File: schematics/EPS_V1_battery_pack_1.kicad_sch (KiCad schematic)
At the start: 31 parts, among them U1 MP2672AGD-0000-Z, U5 MAX17205G+

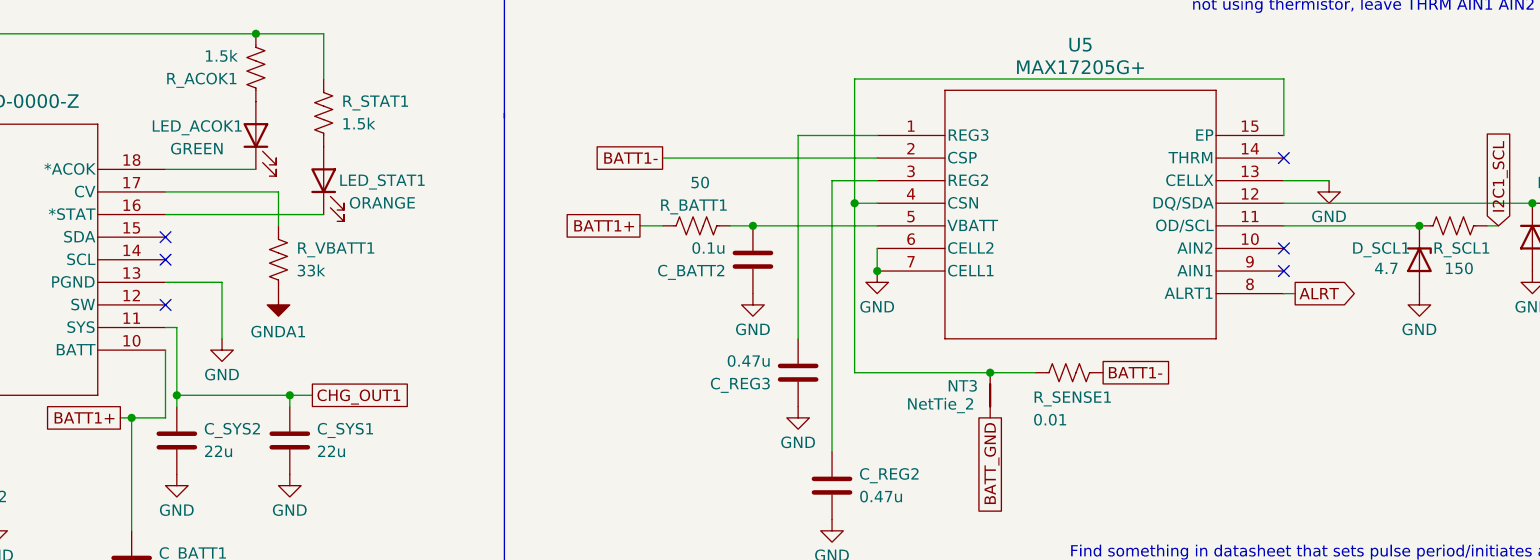
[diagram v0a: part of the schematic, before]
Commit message: Fix NC pins, add 2 test points & silkscreen labels
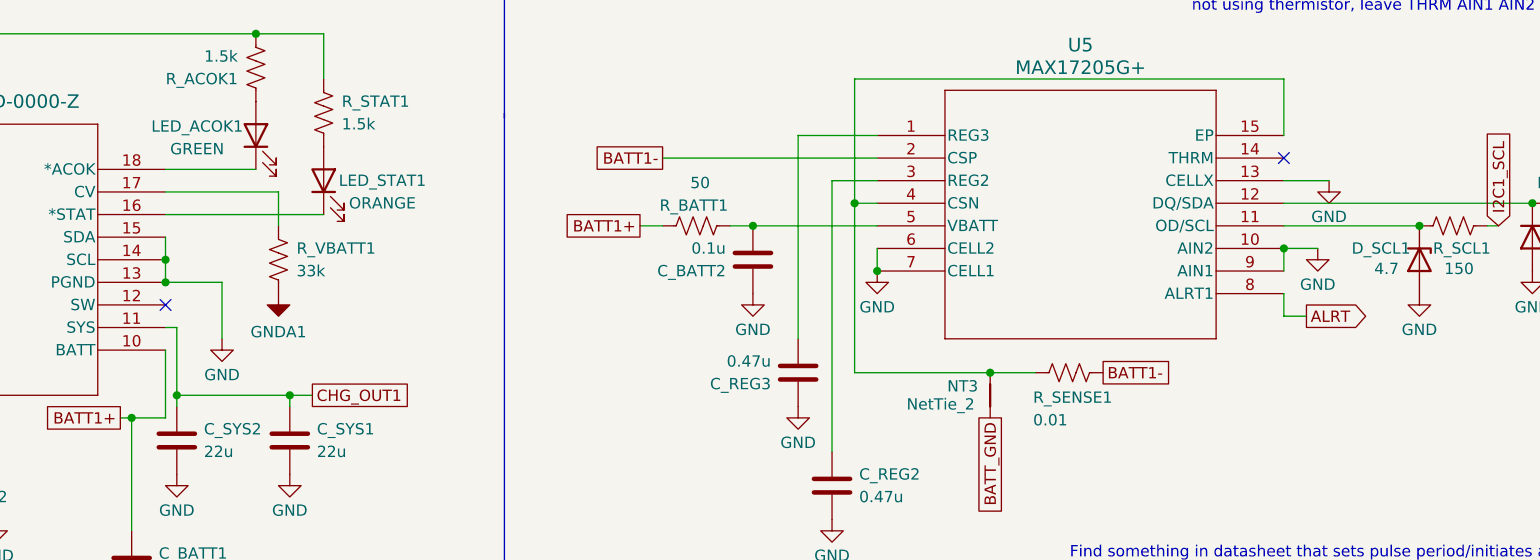
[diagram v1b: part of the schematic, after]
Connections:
- net GND: now also U1.14 (SCL), U1.15 (SDA), U5.10 (AIN2), U5.9 (AIN1)
- no-connect marks 6 -> 2
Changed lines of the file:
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@@
+	)
+	(junction
+		(at 104.14 91.44)
+		(diameter 0)
+		(color 0 0 0 0)
 	)
 	(junction
@@
 	)
 	(junction
+		(at 229.87 87.63)
+		(diameter 0)
+		(color 0 0 0 0)
+	)
+	(junction
 		(at 170.18 85.09)
 		(diameter 0)
@@
 	)
 	(junction
+		(at 104.14 88.9)
+		(diameter 0)
+		(color 0 0 0 0)
+	)
+	(junction
 		(at 50.8 96.52)
 		(diameter 0)
@@
 	)
 	(no_connect
-		(at 229.87 90.17)
-	)
-	(no_connect
 		(at 104.14 93.98)
-	)
-	(no_connect
-		(at 104.14 88.9)
-	)
-	(no_connect
-		(at 104.14 86.36)
 	)
 	(no_connect
 		(at 229.87 77.47)
 	)
-	(no_connect
-		(at 229.87 87.63)
-	)
 	(wire
 		(pts
@@
 	(wire
 		(pts
+			(xy 229.87 87.63) (xy 233.68 87.63)
+		)
+		(stroke
+			(width 0)
+			(type default)
+		)
+	)
+	(wire
+		(pts
 			(xy 50.8 86.36) (xy 63.5 86.36)
 		)
@@
 	(wire
 		(pts
+			(xy 104.14 86.36) (xy 104.14 88.9)
+		)
+		(stroke
+			(width 0)
+			(type default)
+		)
+	)
+	(wire
+		(pts
 			(xy 170.18 85.09) (xy 184.15 85.09)
 		)
@@
 		)
 	)
+	(wire
+		(pts
+			(xy 229.87 95.25) (xy 229.87 92.71)
+		)
+		(stroke
+			(width 0)
+			(type default)
+		)
+	)
 	(polyline
 		(pts
@@
 	(wire
 		(pts
+			(xy 229.87 87.63) (xy 229.87 90.17)
+		)
+		(stroke
+			(width 0)
+			(type default)
+		)
+	)
+	(wire
+		(pts
 			(xy 50.8 96.52) (xy 50.8 95.25)
 		)
@@
 	(wire
 		(pts
-			(xy 229.87 92.71) (xy 231.14 92.71)
-		)
-		(stroke
-			(width 0)
-			(type default)
-		)
-	)
-	(wire
-		(pts
 			(xy 104.14 83.82) (xy 121.92 83.82)
 		)
@@
 	(wire
 		(pts
+			(xy 229.87 95.25) (xy 232.41 95.25)
+		)
+		(stroke
+			(width 0)
+			(type default)
+		)
+	)
+	(wire
+		(pts
 			(xy 29.21 93.98) (xy 63.5 93.98)
 		)
@@
 		(pts
 			(xy 114.3 63.5) (xy 48.26 63.5)
+		)
+		(stroke
+			(width 0)
+			(type default)
+		)
+	)
+	(wire
+		(pts
+			(xy 104.14 88.9) (xy 104.14 91.44)
 		)
 		(stroke
@@
 	(global_label "ALRT"
 		(shape output)
-		(at 231.14 92.71 0)
+		(at 232.41 95.25 0)
 		(fields_autoplaced yes)
 		(effects
@@
 		)
 		(property "Intersheetrefs" "${INTERSHEET_REFS}"
-			(at 238.4795 92.71 0)
+			(at 239.7495 95.25 0)
 			(hide yes)
 			(show_name no)
@@
 					(unit 1)
 				)
+			)
+		)
+	)
+	(symbol
+		(lib_id "power:GND")
+		(at 233.68 87.63 0)
+		(unit 1)
+		(body_style 1)
+		(exclude_from_sim no)
+		(in_bom yes)
+		(on_board yes)
+		(in_pos_files yes)
+		(dnp no)
+		(property "Reference" "#PWR0130"
+			(at 233.68 93.98 0)
+			(hide yes)
+			(show_name no)
+			(do_not_autoplace no)
+			(effects
+				(font
+					(size 1.27 1.27)
+				)
+			)
+		)
+		(property "Value" "GND"
+			(at 233.68 91.694 0)
+			(show_name no)
+			(do_not_autoplace no)
+			(effects
+				(font
+					(size 1.27 1.27)
+				)
+			)
+		)
+		(property "Footprint" ""
+			(at 233.68 87.63 0)
+			(hide yes)
+			(show_name no)
+			(do_not_autoplace no)
+			(effects
+				(font
+					(size 1.27 1.27)
+				)
+			)
+		)
+		(property "Datasheet" ""
+			(at 233.68 87.63 0)
+			(hide yes)
+			(show_name no)
+			(do_not_autoplace no)
+			(effects
+				(font
+					(size 1.27 1.27)
+				)
+			)
+		)
+		(property "Description" "Power symbol creates a global label with name \"GND\" , ground"
+			(at 233.68 87.63 0)
+			(hide yes)
+			(show_name no)
+			(do_not_autoplace no)
+			(effects
+				(font
+					(size 1.27 1.27)
+				)
+			)
+		)
+		(pin "1"
+		)
+		(instances
+			(project "EPS_V1"
+				(path "/85157432-5d03-48fa-ab40-27ed3d133f47/d6a7ca1d-fe68-467f-8233-74a5cf811189"
+					(reference "#PWR0130")
+					(unit 1)
+				)

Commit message: Fix silkscreen; Fix component value style
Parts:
- C_BATT2, C_BST1: value 0.1u -> 100n
- C_REG2, C_REG3: value 0.47u -> 470n
- R_BATT1, R_MID1: value 50 -> 50R
- R_SCL1, R_SDA1: value 150 -> 150R
- R_SENSE1: value 0.01 -> 10m
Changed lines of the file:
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@@
 			)
 		)
-		(property "Value" "150"
+		(property "Value" "150R"
 			(at 263.144 77.724 90)
 			(show_name no)
@@
 			)
 		)
-		(property "Value" "0.1u"
+		(property "Value" "100n"
 			(at 167.132 87.63 0)
 			(show_name no)
@@
 			)
 		)
-		(property "Value" "150"
+		(property "Value" "150R"
 			(at 247.904 89.916 90)
 			(show_name no)
@@
 			)
 		)
-		(property "Value" "50"
+		(property "Value" "50R"
 			(at 165.354 80.264 90)
 			(show_name no)
@@
 			)
 		)
-		(property "Value" "0.01"
+		(property "Value" "10m"
 			(at 201.676 106.934 90)
 			(show_name no)
@@
 			)
 		)
-		(property "Value" "50"
+		(property "Value" "50R"
 			(at 61.722 101.6 0)
 			(show_name no)
@@
 			)
 		)
-		(property "Value" "0.47u"
+		(property "Value" "470n"
 			(at 172.212 100.33 0)
 			(show_name no)
@@
 			)
 		)
-		(property "Value" "0.1u"
+		(property "Value" "100n"
 			(at 55.118 78.74 0)
 			(show_name no)
@@
 			)
 		)
-		(property "Value" "0.47u"
+		(property "Value" "470n"
 			(at 182.118 115.57 0)
 			(show_name no)

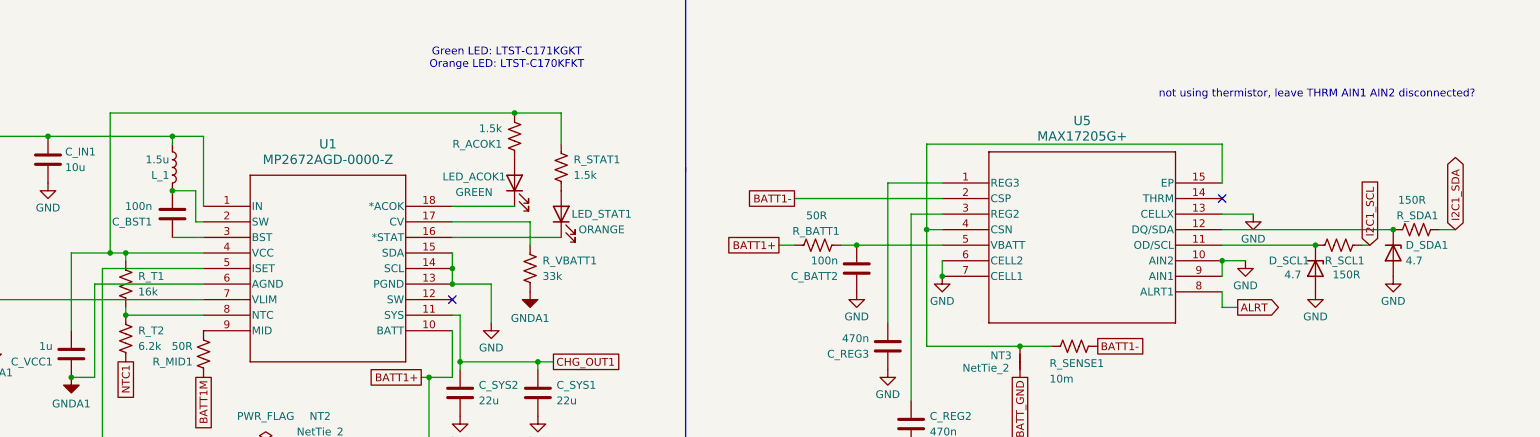
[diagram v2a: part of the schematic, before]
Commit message: Switch out MP28167 for LTC3119 (MPPC buck-boost) in schematic
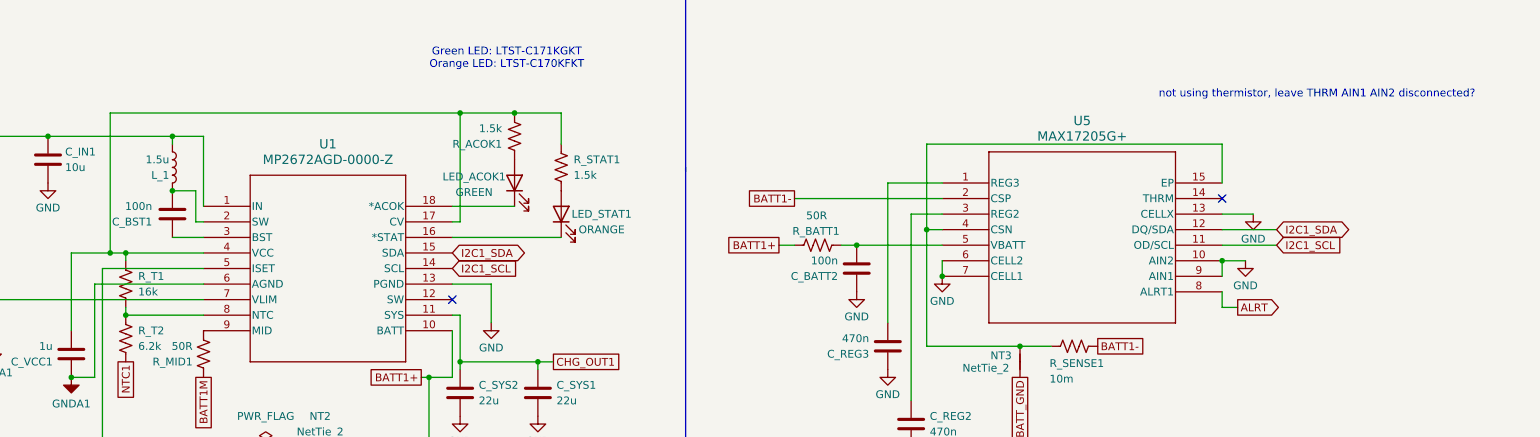
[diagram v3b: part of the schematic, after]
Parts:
- removed D_SCL1, D_SDA1: 4.7, Diode_SMD:D_0603_1608Metric, symbol Device:D_Zener
- removed R_SCL1, R_SDA1: 150R, Resistor_SMD:R_0603_1608Metric, symbol Device:R_US
- removed R_VBATT1: 33k, Resistor_SMD:R_0603_1608Metric, symbol Device:R_US
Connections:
- net GND: no longer U1.14 (SCL), U1.15 (SDA)
- net I2C1_SCL: now also U1.14 (SCL), U5.11 (OD/SCL)
- net I2C1_SDA: now also U1.15 (SDA), U5.12 (DQ/SDA)
- net at U1.17 (CV): now also C_VCC1.2, R_ACOK1.2, R_STAT1.1, R_T1.1, U1.4 (VCC)

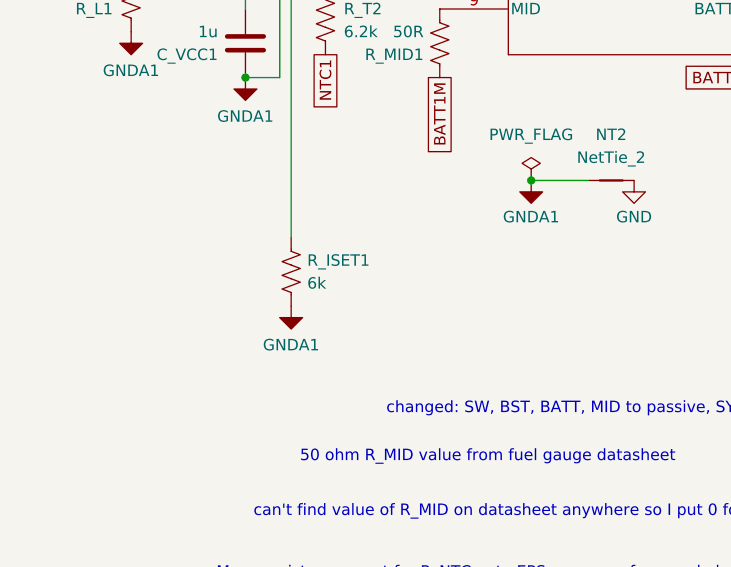
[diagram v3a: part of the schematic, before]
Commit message: fix U6 EN pin, add ALRT pullup R, update 3dmodels, regen step
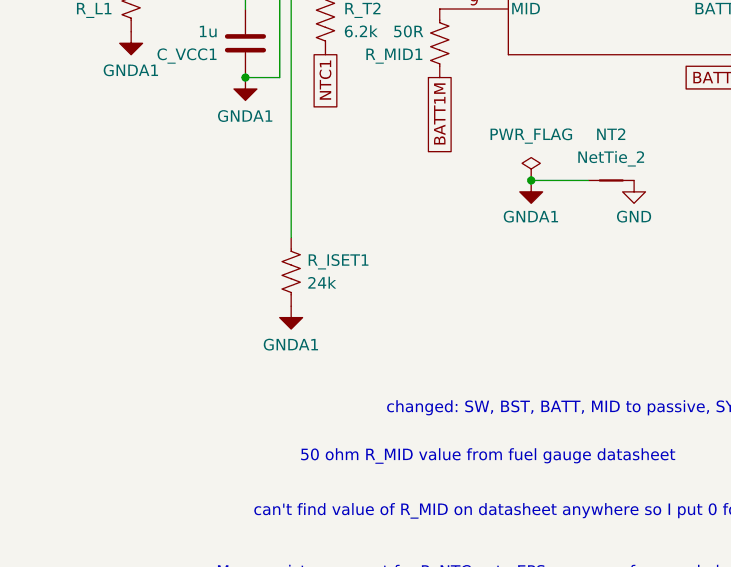
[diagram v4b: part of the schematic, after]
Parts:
- R_ISET1: value 6k -> 24k
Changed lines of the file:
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@@
 			)
 		)
-		(property "Value" "6k"
+		(property "Value" "24k"
 			(at 48.768 129.54 0)
 			(show_name no)
